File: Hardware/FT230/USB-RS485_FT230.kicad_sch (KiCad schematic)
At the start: 36 parts, among them J2 7-pin con, J3 3.3 LVL 5, J6 USB_C_Receptacle_USB2.0_16P, Q1 BC857, U1 FT230XQ, U2 SN75176AD, U3 AMS1117-3.3, U4 DC-DC, U5 EL817, U6 EL817

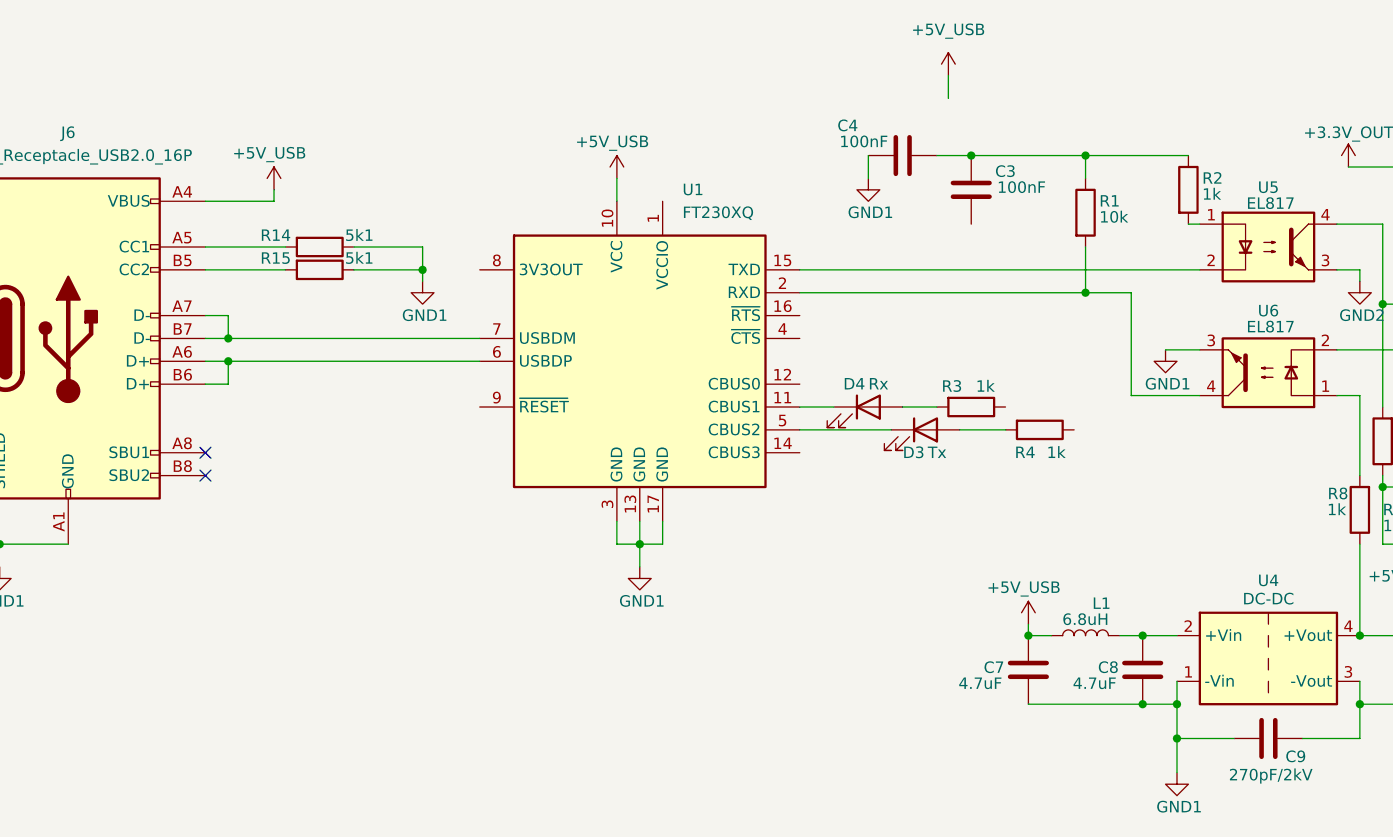
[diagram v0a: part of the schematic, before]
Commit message: FT230 schematics
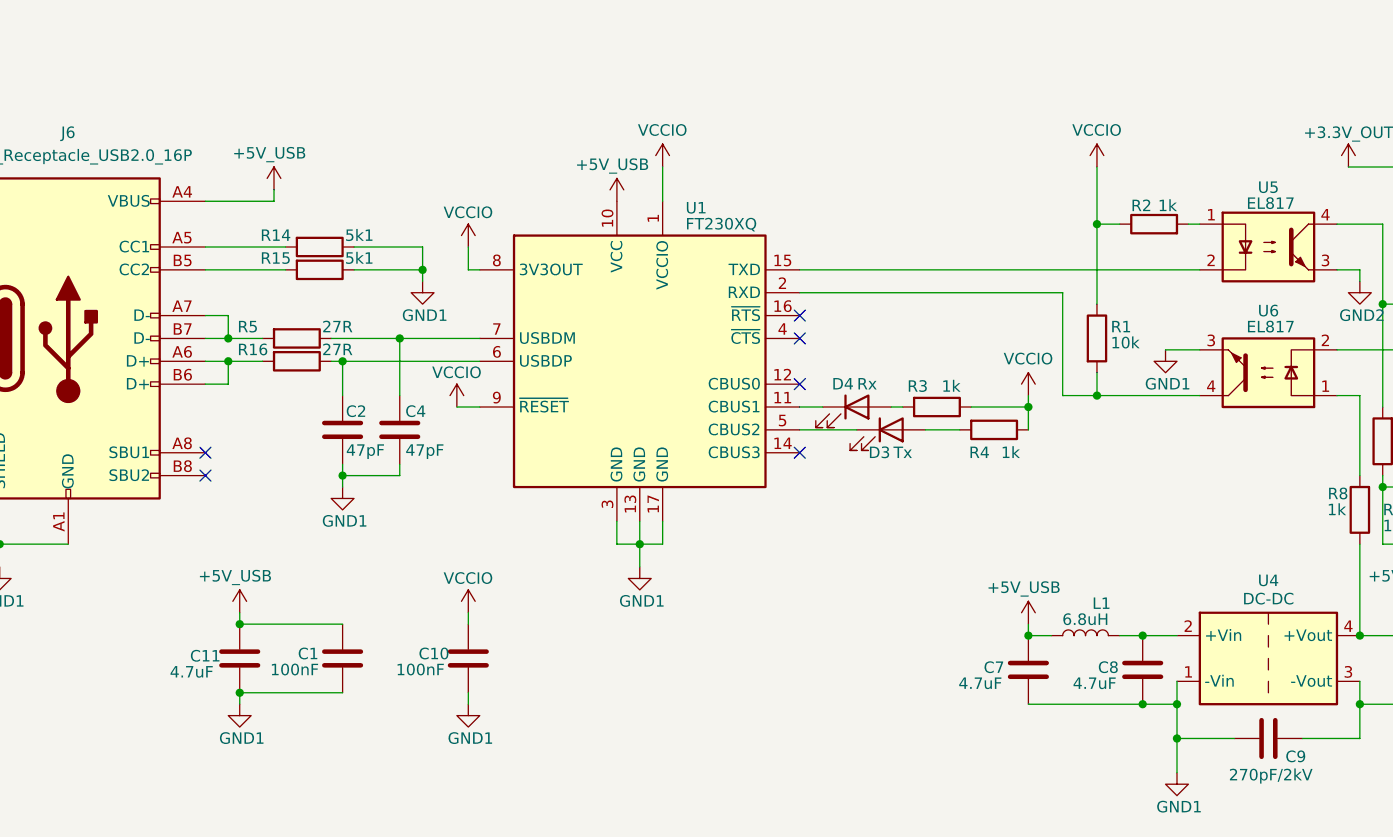
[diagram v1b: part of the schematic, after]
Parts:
- removed C3: 100nF, Capacitor_SMD:C_0805_2012Metric, symbol Device:C
- added C1, C10: 100nF, Capacitor_SMD:C_0805_2012Metric, symbol Device:C
- added C11: 4.7uF, Capacitor_SMD:C_0805_2012Metric, symbol Device:C
- added C2: 47pF, Capacitor_SMD:C_0805_2012Metric, symbol Device:C
- added R16, R5: 27R, Resistor_SMD:R_0805_2012Metric, symbol Device:R
- C4: value 100nF -> 47pF; LCSC PN C14663 -> (none); MF PN CC0603KRX7R9BB104 -> 885012007032; Manufacturer (none) -> Wurth Elektronik
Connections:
- net +5V_USB: now also C1.1, C11.2
- net GND1: now also C1.2, C10.2, C11.1, C2.2
- net VCCIO: now reaches R3.1
- net VCCIO: now also R1.1, R2.1, R4.1, U1.1 (VCCIO), U1.8 (3V3OUT), U1.9 (~{RESET}), C10.1
- net at J6.A6 (D+), J6.B6 (D+): now also R16.2; no longer U1.6 (USBDP)
- net at J6.A7 (D-), J6.B7 (D-): now also R5.2; no longer U1.7 (USBDM)
- new net: C2.1, R16.1, U1.6 (USBDP)
- new net: C4.1, R5.1, U1.7 (USBDM)
- no-connect marks 2 -> 6
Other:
- moved on the sheet: D3, D4, R3, R4

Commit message: FT230 PCB - in progress
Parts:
- renumbered C11 to C1, C6 to C10, C1 to C3, C10 to C5, C7 to C6, C8 to C7, C9 to C8, C5 to C9, D4 to D1, D3 to D2, D2 to D3, D1 to D4, J6 to J1, J3 to J2, J2 to J3, R5 to R1, R12 to R10, R7 to R11, R11 to R12, R9 to R13, R10 to R14, R13 to R15, R6 to R16, R16 to R2, R14 to R3, R15 to R4, R3 to R5, R4 to R6, R1 to R7, R2 to R8, R8 to R9, U5 to U2, U6 to U3, U3 to U5, U2 to U6

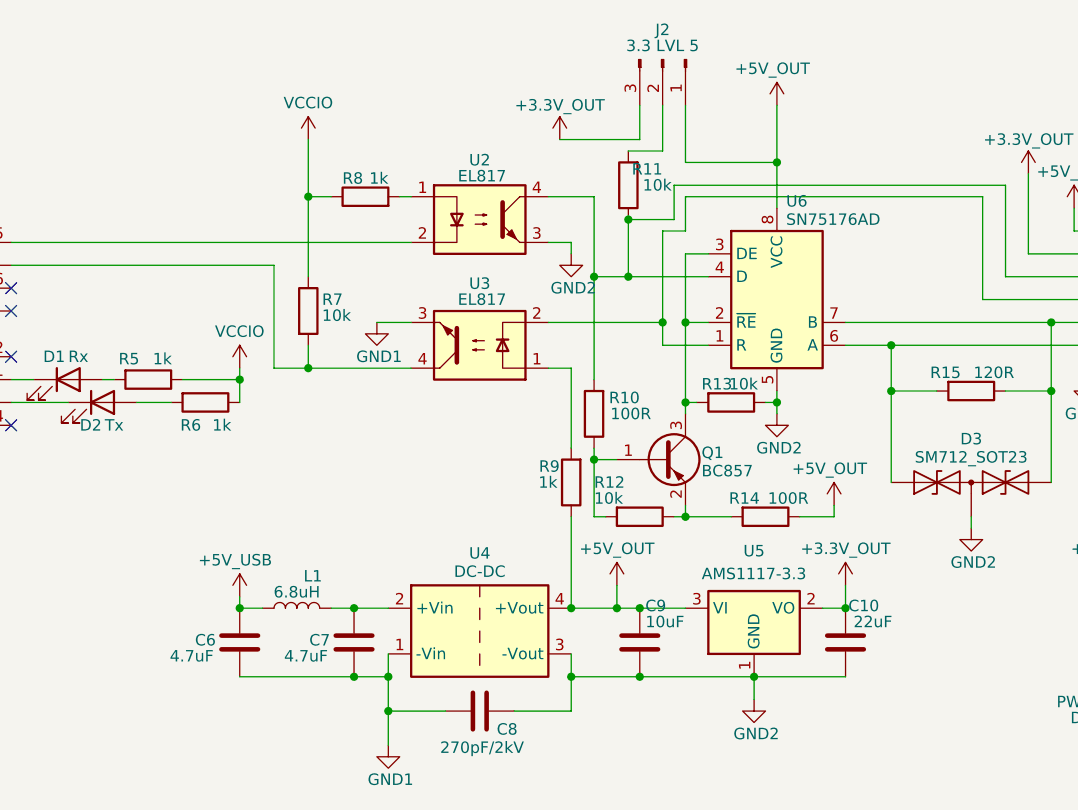
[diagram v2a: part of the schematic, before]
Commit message: FT230 BOM and fix
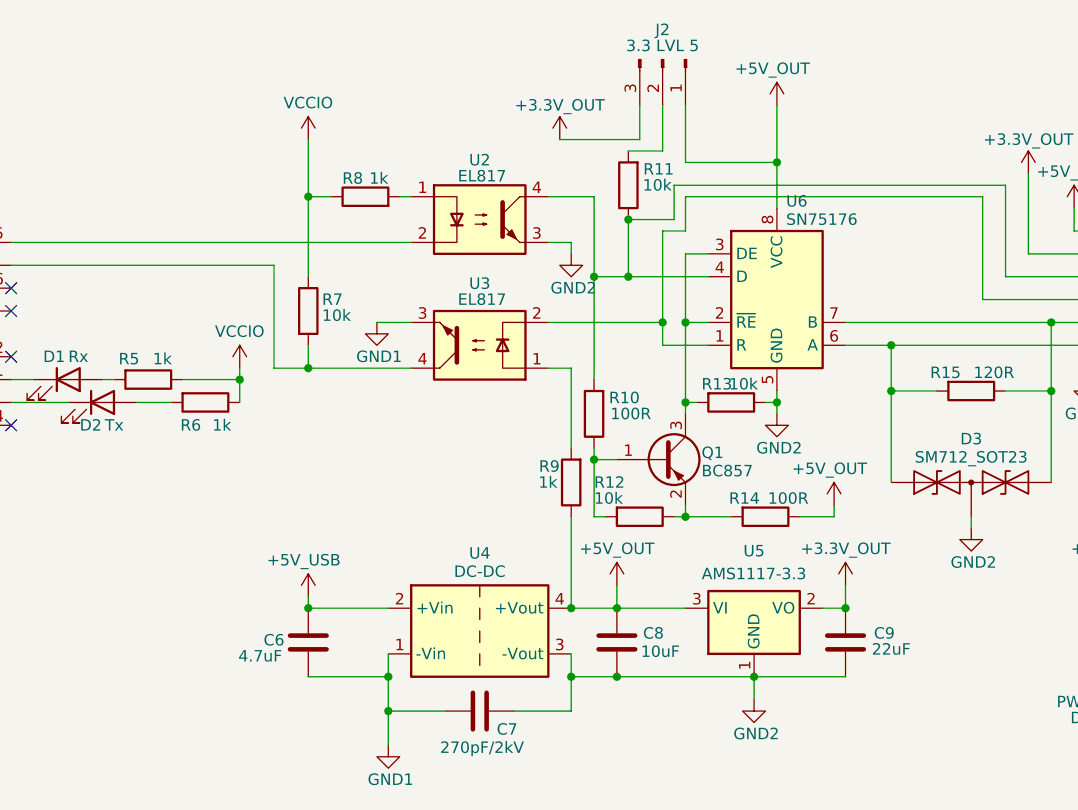
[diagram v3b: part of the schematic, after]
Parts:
- removed C7: 4.7uF, Capacitor_SMD:C_0805_2012Metric, symbol Device:C
- removed L1: 6.8uH, Inductor_SMD:L_1206_3216Metric, symbol Device:L
- C1, C6: LCSC PN C2858031 -> (none); MF PN GRM155R61E475ME15D -> (none); MPN (none) -> 885012207053; Manufacturer (none) -> Wurth Elektronik
- C3, C5: LCSC PN C14663 -> (none); MF PN CC0603KRX7R9BB104 -> (none); MPN (none) -> 885012207098; Manufacturer (none) -> Wurth Elektronik
- C4: MF PN 885012007032 -> (none); MPN (none) -> 885012007032
- C7: renamed from C8; LCSC PN C7393992 -> (none); MF PN TCC1206X7R271K202FT -> (none); MPN (none) -> C1206C271MGRACTU; Manufacturer (none) -> KEMET
- C8: renamed from C9; LCSC PN C315248 -> (none); MF PN CL05A106MP5NUNC -> (none); MPN (none) -> 885012107004; Manufacturer (none) -> Wurth Elektronik
- C9: renamed from C10; LCSC PN C415703 -> (none); MF PN GRM155R60J226ME11D -> (none); MPN (none) -> 885012107005; Manufacturer (none) -> Wurth Elektronik
- D1: MPN (none) -> 150080YS75000; Manufacturer (none) -> Wurth Elektronik
- D2: MPN (none) -> 150224GS73100; Manufacturer (none) -> Wurth Elektronik
- D3: MPN (none) -> SM712-02HTG; Manufacturer (none) -> Littelfuse
- D4: MPN (none) -> 150080RS75000; Manufacturer (none) -> Wurth Elektronik
- J2: MPN (none) -> 77311-127-03LF; Manufacturer (none) -> Amphenol FCI
- J3: MPN (none) -> 10129379-907001BLF; Manufacturer (none) -> Amphenol FCI
- Q1: MPN (none) -> BC857BW-7-F; Manufacturer (none) -> Diodes Incorporated
- R10, R14: MPN (none) -> 560112120020; Manufacturer (none) -> Würth Elektronik
- R11, R12, R13, R7: MPN (none) -> 560112120004; Manufacturer (none) -> Würth Elektronik
- R15: MPN (none) -> CHP0805AFX-1200ELF; Manufacturer (none) -> Bourns
- R16, R5, R6, R8, R9: MPN (none) -> CR0805-FX-1001ELF; Manufacturer (none) -> Bourns
- U1: MPN (none) -> FT230XQ-R; Manufacturer (none) -> FTDI
- U2, U3: LCSC PN C3031553 -> (none); MF PN EL817S1(A)(TU)-FV -> (none); MPN (none) -> DPC817S-B-TR; Manufacturer (none) -> Diodes Incorporated
- U4: LCSC PN C7465178 -> (none); MF PN B0505S-1WR3 -> (none); MPN (none) -> TEA 1-0505; Manufacturer (none) -> TRACO Power
- U5: LCSC PN C110474 -> (none); MF PN AZ1117H-3.3TRG1 -> (none); MPN (none) -> LM1117MPX-3.3/NOPB; Manufacturer (none) -> Texas Instruments
- U6: value SN75176AD -> SN75176; LCSC PN C7063 -> (none); MF PN SN75176BDR -> (none); MPN (none) -> SN75176BDR; Manufacturer (none) -> Texas Instruments
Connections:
- net +5V_USB: now also U4.2 (+Vin)
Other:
- moved on the sheet: C6, C8

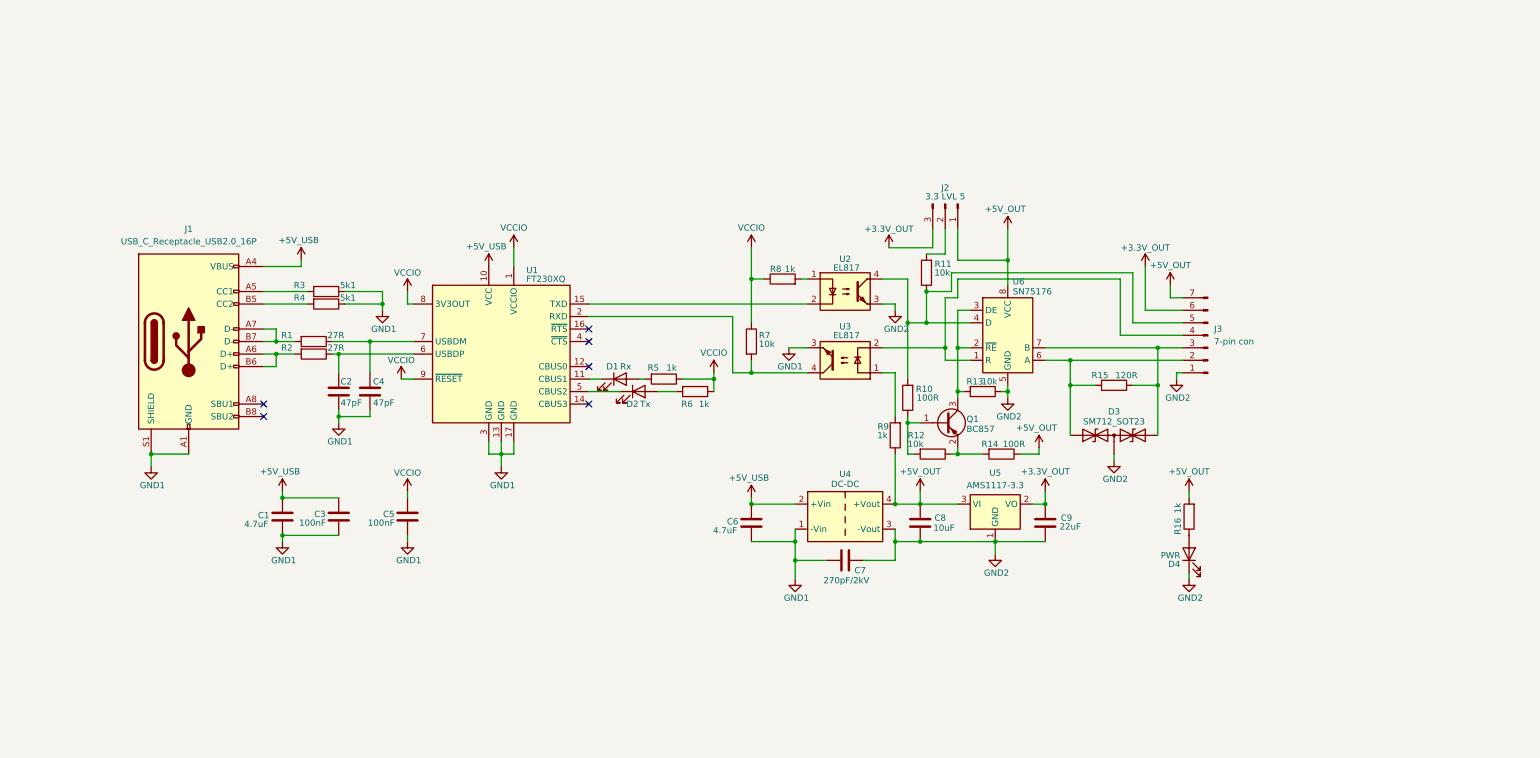
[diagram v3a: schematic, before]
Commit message: schematics cosmetic change
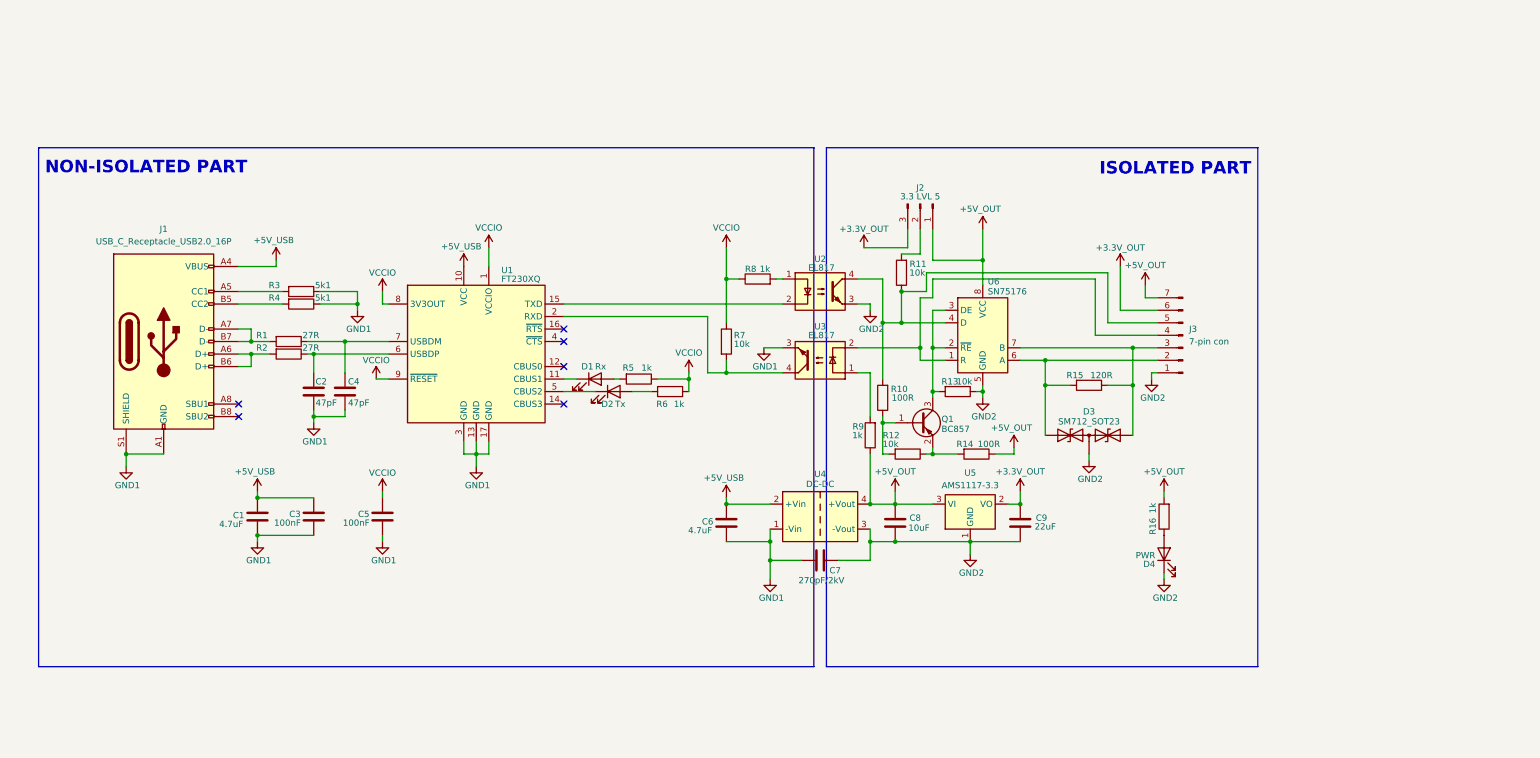
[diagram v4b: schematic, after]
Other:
- note added: "ISOLATED PART"
- note added: "NON-ISOLATED PART"
- moved on the sheet: C1, C2, C3, C4, C5, C6, C7, C8, C9, D1, D2, D3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

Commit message: -opto +Adum & 1.8
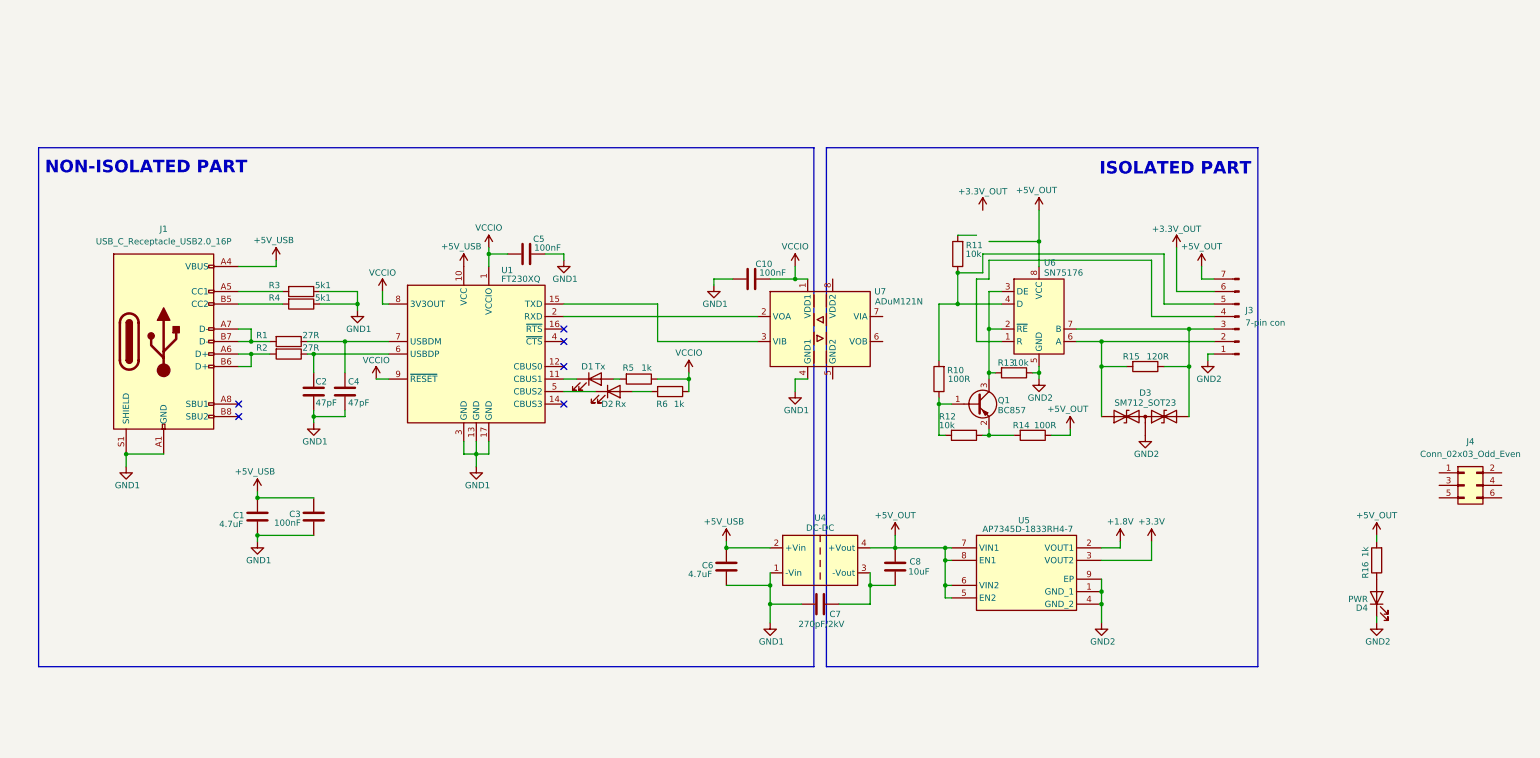
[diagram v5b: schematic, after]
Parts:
- removed C9: 22uF, Capacitor_SMD:C_0805_2012Metric, symbol Device:C
- removed J2: 3.3 LVL 5, Connector_PinHeader_2.54mm:PinHeader_1x03_P2.54mm_Vertical, symbol Connector:Conn_01x03_Pin
- removed R7: 10k, Resistor_SMD:R_0805_2012Metric, symbol Device:R
- removed R8, R9: 1k, Resistor_SMD:R_0805_2012Metric, symbol Device:R
- removed U2, U3: EL817, Package_DIP:SMDIP-4_W9.53mm, symbol Isolator:LTV-817S
- removed U5: AMS1117-3.3, Package_TO_SOT_SMD:SOT-223-3_TabPin2, symbol Regulator_Linear:AMS1117-3.3
- added C10: 100nF, Capacitor_SMD:C_0805_2012Metric, symbol Device:C
- added J4: Conn_02x03_Odd_Even, Connector_PinHeader_1.00mm:PinHeader_2x03_P1.00mm_Vertical, symbol Connector_Generic:Conn_02x03_Odd_Even
- added U5: AP7345D-1833RH4-7, AP7345D1833RH47, symbol AP7345D-1833RH4-7:AP7345D-1833RH4-7
- added U7: ADuM121N, Package_SO:SOIC-8_3.9x4.9mm_P1.27mm, symbol Isolator:ADuM121N
- D1: value Rx -> Tx
- D2: value Tx -> Rx
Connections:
- net +5V_OUT: now also U5.5 (EN2), U5.6 (VIN2), U5.7 (VIN1), U5.8 (EN1)
- net GND1: now also C10.1, U7.4 (GND1)
- net GND2: now also U5.1 (GND_1), U5.4 (GND_2), U5.9 (EP); no longer C7.2, C8.1, U4.3 (-Vout)
- net VCCIO: now also C10.2, U7.1 (VDD1)
- net at U1.2 (RXD): now also U7.2 (VOA)
- net at U1.15 (TXD): now also U7.3 (VIB)
- new net: C7.2, C8.1, U4.3 (-Vout)
- new net +1.8V: U5.2 (VOUT1)
- new net +3.3V: U5.3 (VOUT2)
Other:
- moved on the sheet: C5, C6, C7, C8, D3, D4, J3, Q1, R10, R11, R12, R13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
